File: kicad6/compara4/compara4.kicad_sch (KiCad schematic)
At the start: 67 parts, among them J1 In_1, J2 In_2, J3 In_3, J4 In_4, J5 CV_Jack, J6 Out_OR, J7 Out_NOR, J8 Out_XOR, J9 Out_XNOR, Q1 BC547, Q2 BC547, Q3 BC547, Q4 BC547, SW1 SW_SPDT, U1 TL074, U2 4070, U3 4041

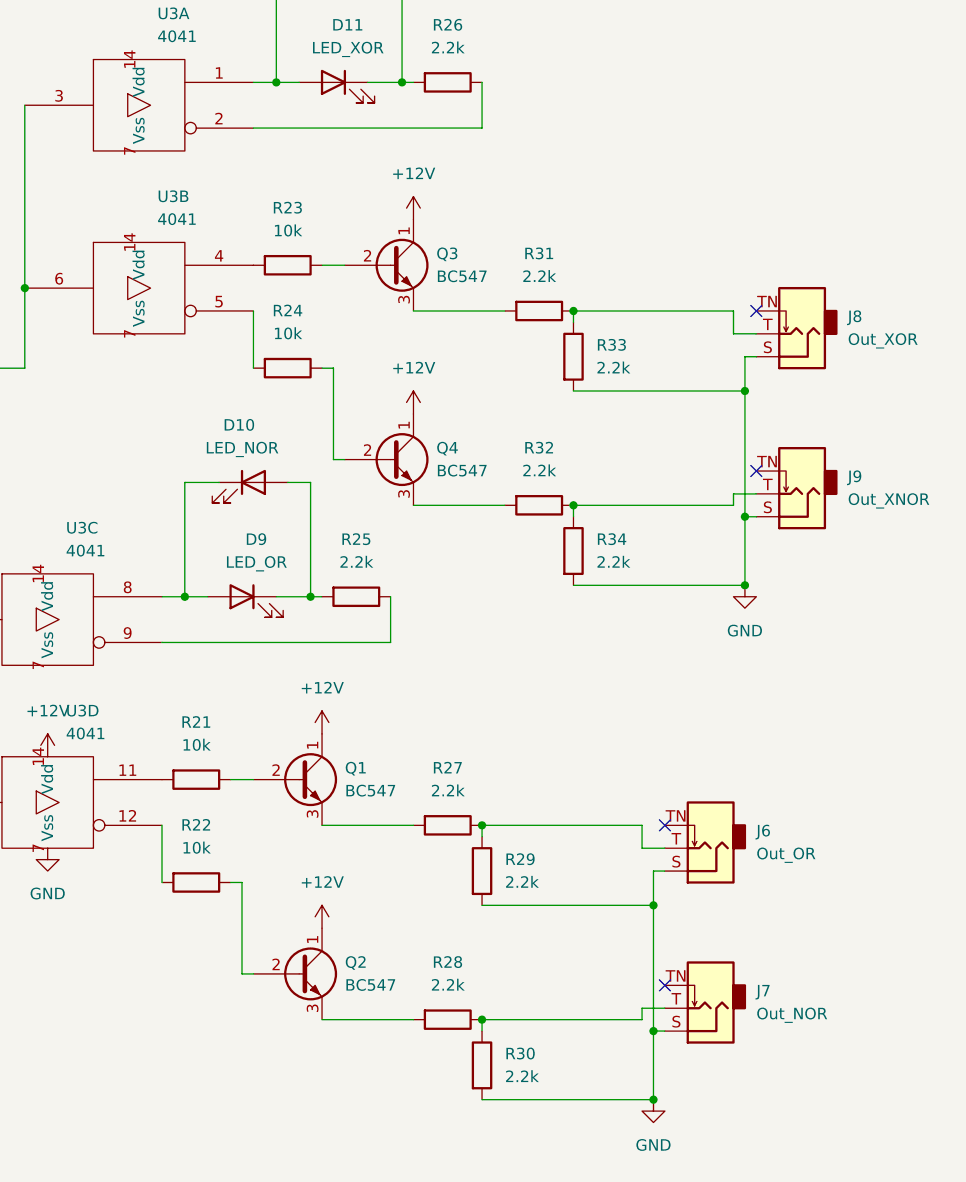
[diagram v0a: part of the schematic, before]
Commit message: Remove transistors from Compara4 schematic
- CD4041 can drive 500 mW total Each LED through 2.2V is about 65 mW
- With potential divider to reduce output voltage, the power numbers for shorts get less scary than through 1k directly.
- If gate output is shorted to ground through 2.2k resistor, it's effectively just another LED - no problem.
- In a worst-case short to -12V, 130mW are drawn from CD4041. This would push it hard but probably not burn it out quickly.
- The resistor between CD4041 and output "sees" twice the voltage drop and passes >1/4W. If this (or an additional low-value series resistor) is specified as a 1/8W then it could act as an additional protection "fuse".
- Probably unnecessary as we don't expect to see simultanous shorts to -12V.
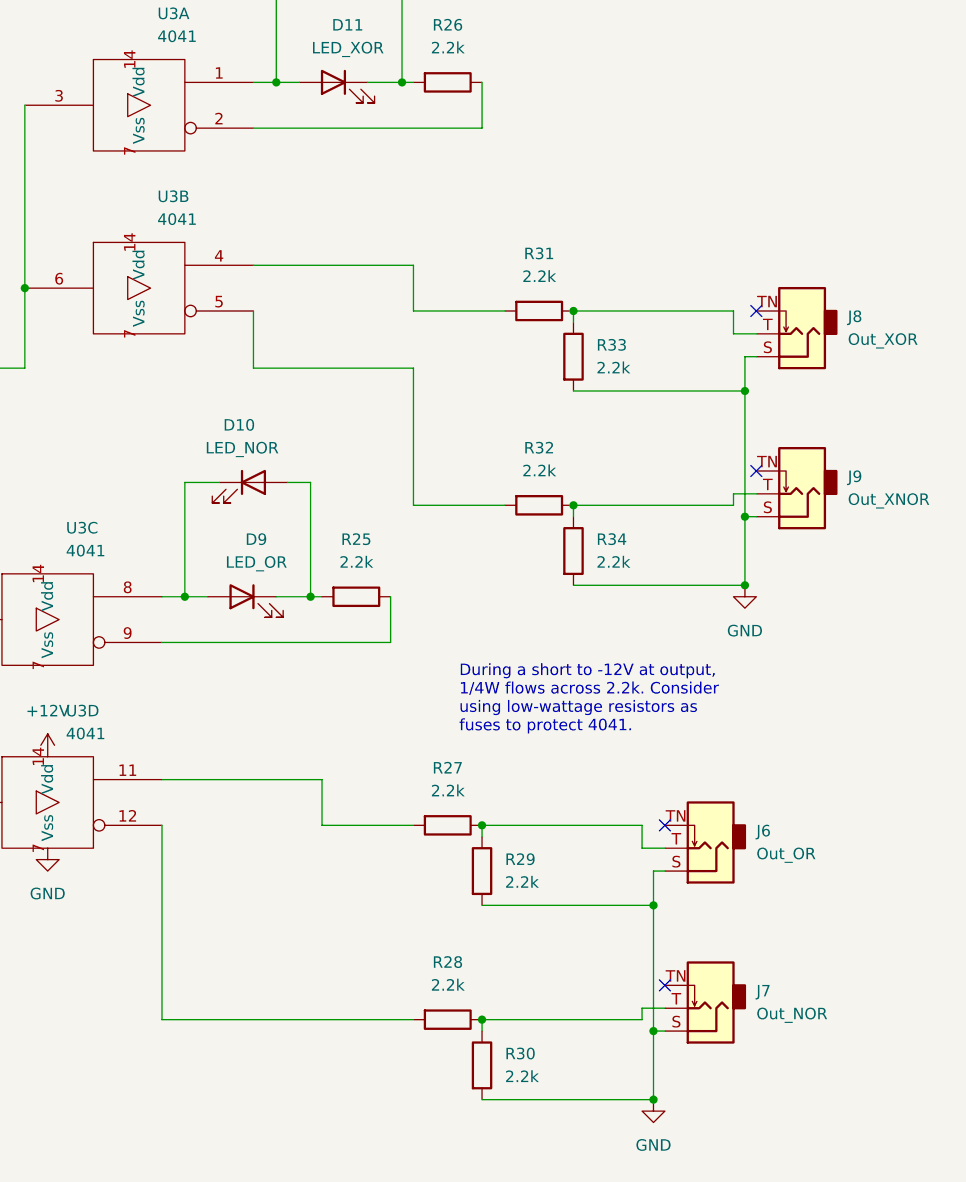
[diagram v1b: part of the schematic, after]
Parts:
- removed Q1, Q2, Q3, Q4: BC547, Package_TO_SOT_THT:TO-92_Inline, symbol Transistor_BJT:BC547
- removed R21, R22, R23, R24: 10k, Resistor_THT:R_Axial_DIN0207_L6.3mm_D2.5mm_P7.62mm_Horizontal, symbol Device:R
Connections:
- net at R32.2: now also U3.5
- net at R31.2: now also U3.4
- net at R28.2: now also U3.12
- net at R27.2: now also U3.11
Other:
- note added: "During a short to -12V at output, 1/4W flows across 2.2k. Consider using low-wattage resistors as fuses to protect 4041."

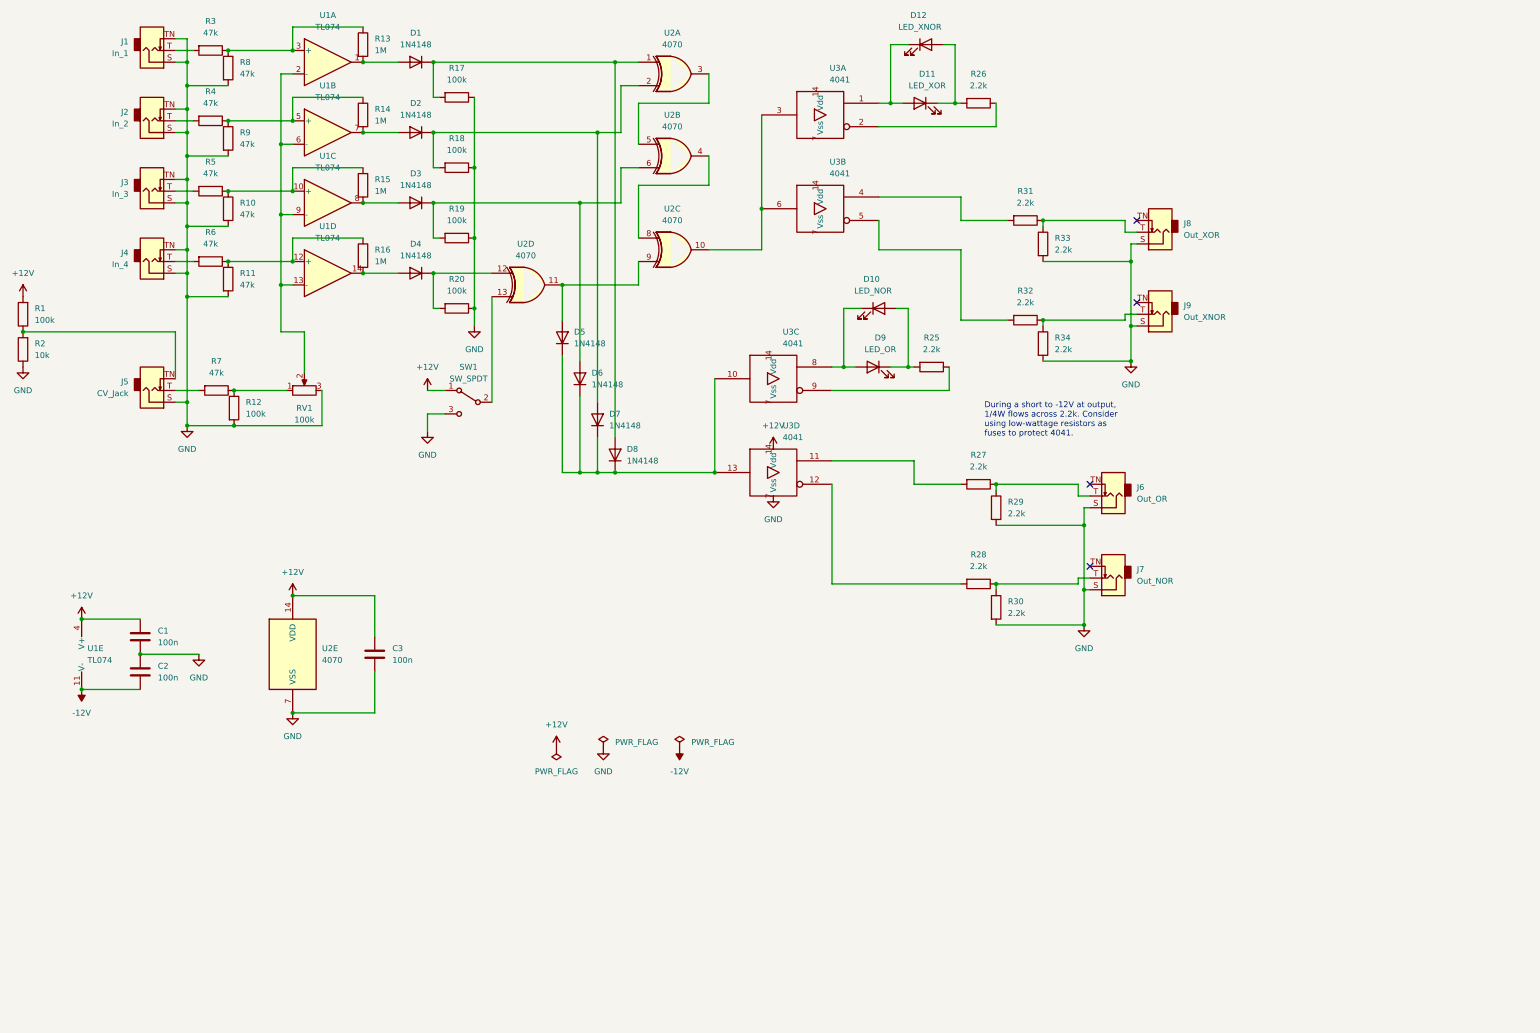
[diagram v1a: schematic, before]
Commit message: compara4; breakout controls, layout for perfboard
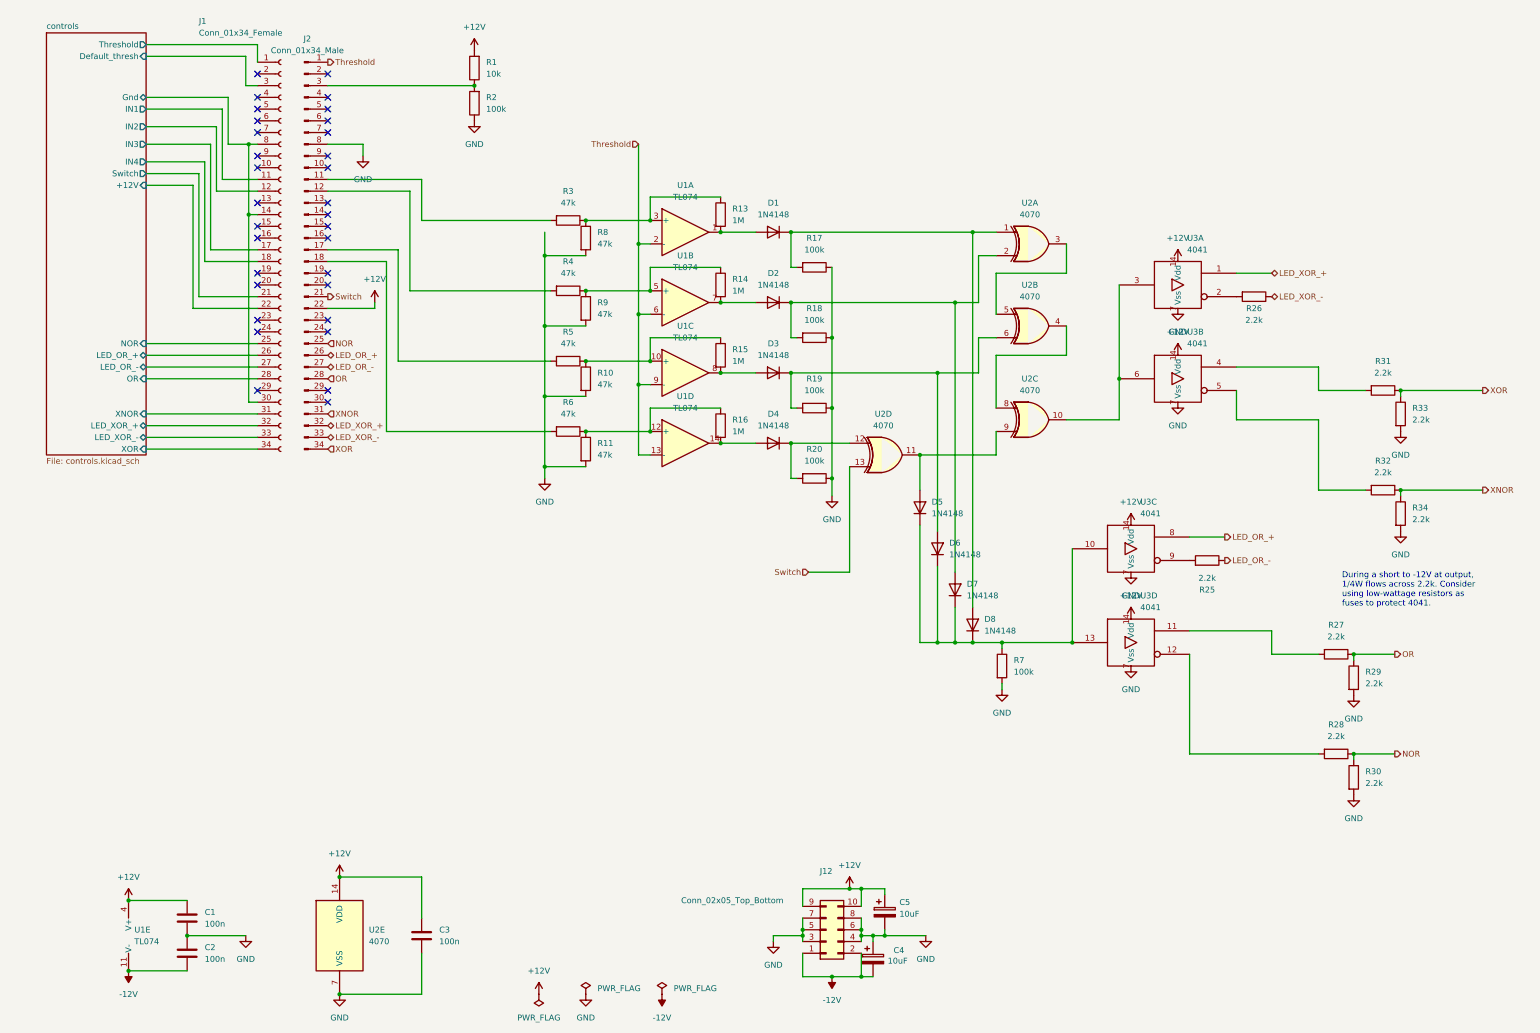
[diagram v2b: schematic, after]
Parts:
- removed D10: LED_NOR, LED_THT:LED_D3.0mm_FlatTop, symbol Device:LED
- removed D11: LED_XOR, LED_THT:LED_D3.0mm_FlatTop, symbol Device:LED
- removed D12: LED_XNOR, LED_THT:LED_D3.0mm_FlatTop, symbol Device:LED
- removed D9: LED_OR, LED_THT:LED_D3.0mm_FlatTop, symbol Device:LED
- removed J1: In_1, Connector_Audio:Jack_3.5mm_QingPu_WQP-PJ398SM_Vertical_CircularHoles, symbol Connector:AudioJack2_SwitchT
- removed J2: In_2, Connector_Audio:Jack_3.5mm_QingPu_WQP-PJ398SM_Vertical_CircularHoles, symbol Connector:AudioJack2_SwitchT
- removed J3: In_3, Connector_Audio:Jack_3.5mm_QingPu_WQP-PJ398SM_Vertical_CircularHoles, symbol Connector:AudioJack2_SwitchT
- removed J4: In_4, Connector_Audio:Jack_3.5mm_QingPu_WQP-PJ398SM_Vertical_CircularHoles, symbol Connector:AudioJack2_SwitchT
- removed J5: CV_Jack, Connector_Audio:Jack_3.5mm_QingPu_WQP-PJ398SM_Vertical_CircularHoles, symbol Connector:AudioJack2_SwitchT
- removed J6: Out_OR, Connector_Audio:Jack_3.5mm_QingPu_WQP-PJ398SM_Vertical_CircularHoles, symbol Connector:AudioJack2_SwitchT
- removed J7: Out_NOR, Connector_Audio:Jack_3.5mm_QingPu_WQP-PJ398SM_Vertical_CircularHoles, symbol Connector:AudioJack2_SwitchT
- removed J8: Out_XOR, Connector_Audio:Jack_3.5mm_QingPu_WQP-PJ398SM_Vertical_CircularHoles, symbol Connector:AudioJack2_SwitchT
- removed J9: Out_XNOR, Connector_Audio:Jack_3.5mm_QingPu_WQP-PJ398SM_Vertical_CircularHoles, symbol Connector:AudioJack2_SwitchT
- removed R12: 100k, Resistor_THT:R_Axial_DIN0207_L6.3mm_D2.5mm_P7.62mm_Horizontal, symbol Device:R
- removed RV1: 100k, Potentiometer_THT:Potentiometer_Alpha_RD901F-40-00D_Single_Vertical, symbol Device:R_Potentiometer
- removed SW1: SW_SPDT, Library:Dailywell sub-miniature toggle switch, symbol Switch:SW_SPDT
- added C4, C5: 10uF, Capacitor_THT:CP_Radial_D5.0mm_P2.50mm, symbol Device:C_Polarized
- added J1: Conn_01x34_Female, Connector_PinHeader_2.54mm:PinHeader_1x34_P2.54mm_Vertical, symbol Connector:Conn_01x34_Female
- added J12: Conn_02x05_Top_Bottom, Connector_IDC:IDC-Header_2x05_P2.54mm_Vertical, symbol Connector_Generic:Conn_02x05_Odd_Even
- added J2: Conn_01x34_Male, Connector_PinHeader_2.54mm:PinHeader_1x34_P2.54mm_Horizontal, symbol Connector:Conn_01x34_Male
- R1: value 100k -> 10k
- R2: value 10k -> 100k
- R7: value 47k -> 100k
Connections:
- net +12V: now also U3.14 (Vdd), U3.14 (Vdd), U3.14 (Vdd), C5.1, J12.10 (Pin_10), J12.9 (Pin_9), J2.22 (Pin_22)
- net -12V: now also C4.2, J12.1 (Pin_1), J12.2 (Pin_2)
- net GND: now also R7.2, U3.7 (Vss), U3.7 (Vss), U3.7 (Vss), C4.1, C5.2, J12.3 (Pin_3), J12.4 (Pin_4), J12.5 (Pin_5), J12.6 (Pin_6), J12.7 (Pin_7), J12.8 (Pin_8), J2.8 (Pin_8)
- net XNOR: now reaches R32.1, R34.1
- net XNOR: now also J2.31 (Pin_31)
- net LED_XOR_+: now reaches U3.1
- net LED_XOR_+: now also J2.32 (Pin_32)
- net at R26.2: now also U3.2
- net at D5.1 (K), D6.1 (K), D7.1 (K)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: now also R7.1
- net XOR: now reaches R31.1, R33.1
- net XOR: now also J2.34 (Pin_34)
- net NOR: now reaches R28.1, R30.1
- net NOR: now also J2.25 (Pin_25)
- net Switch: now reaches U2.13
- net Switch: now also J2.21 (Pin_21)
- net Threshold: now reaches U1.13 (-), U1.2 (-), U1.6 (-), U1.9 (-)
- net Threshold: now also J2.1 (Pin_1)
- net OR: now reaches R27.1, R29.1
- net OR: now also J2.28 (Pin_28)
- net at R1.1, R2.2: now also J2.3 (Pin_3)
- net at R4.2: now also J2.12 (Pin_12)
- net at R6.2: now also J2.18 (Pin_18)
- net at R5.2: now also J2.17 (Pin_17)
- net LED_OR_+: now reaches U3.8
- net LED_OR_+: now also J2.26 (Pin_26)
- net at R25.2: now also U3.9
- net at R3.2: now also J2.11 (Pin_11)
- net LED_OR_-: now reaches R25.1
- net LED_OR_-: now also J2.27 (Pin_27); no longer U3.9
- net LED_XOR_-: now reaches R26.1
- net LED_XOR_-: now also J2.33 (Pin_33); no longer U3.2
- new net controls/+12V: J1.22 (Pin_22)
- new net controls/Default_thresh: J1.3 (Pin_3)
- new net controls/Gnd: J1.14 (Pin_14), J1.30 (Pin_30), J1.8 (Pin_8)
- new net controls/IN1: J1.11 (Pin_11)
- new net controls/IN2: J1.12 (Pin_12)
- new net controls/IN3: J1.17 (Pin_17)
- new net controls/IN4: J1.18 (Pin_18)
- new net controls/LED_OR_+: J1.26 (Pin_26)
- new net controls/LED_OR_-: J1.27 (Pin_27)
- new net controls/LED_XOR_+: J1.32 (Pin_32)
- new net controls/LED_XOR_-: J1.33 (Pin_33)
- new net controls/NOR: J1.25 (Pin_25)
- new net controls/OR: J1.28 (Pin_28)
- new net controls/Switch: J1.21 (Pin_21)
- new net controls/Threshold: J1.1 (Pin_1)
- new net controls/XNOR: J1.31 (Pin_31)
- new net controls/XOR: J1.34 (Pin_34)
- no-connect marks 4 -> 32
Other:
- added sheet controls (controls.kicad_sch)
- moved on the sheet: C1, C2, C3, D1, D2, D3, D4, D5, D6, D7, D8, R1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

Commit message: compara4: reverse pot and cleanup ERC
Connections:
- net controls/Gnd: now also J1.24 (Pin_24)
- no-connect marks 32 -> 31
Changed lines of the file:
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@@
   (junction (at 212.09 120.65) (diameter 0) (color 0 0 0 0)
+  )
+  (junction (at 66.675 93.98) (diameter 0) (color 0 0 0 0)
   )
   (junction (at 153.67 85.09) (diameter 0) (color 0 0 0 0)
@@
   (no_connect (at 68.58 50.8))
   (no_connect (at 83.82 43.18))
-  (no_connect (at 68.58 93.98))
   (no_connect (at 68.58 66.04))
   (no_connect (at 68.58 38.1))
@@
     (stroke (width 0) (type default) (color 0 0 0 0))
   )
+  (wire (pts (xy 66.675 93.98) (xy 68.58 93.98))
+    (stroke (width 0) (type default) (color 0 0 0 0))
+  )
   (wire (pts (xy 58.42 76.2) (xy 68.58 76.2))
     (stroke (width 0) (type default) (color 0 0 0 0))
@@
     (stroke (width 0) (type default) (color 0 0 0 0))
   )
-  (wire (pts (xy 66.675 68.58) (xy 66.675 109.22))
+  (wire (pts (xy 66.675 68.58) (xy 66.675 93.98))
     (stroke (width 0) (type default) (color 0 0 0 0))
   )
@@
     (stroke (width 0) (type default) (color 0 0 0 0))
   )
+  (wire (pts (xy 66.675 93.98) (xy 66.675 109.22))
+    (stroke (width 0) (type default) (color 0 0 0 0))
+  )

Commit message: compara4; alignment corrections, some jumper cleanup
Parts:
- added R22: 10k, Resistor_THT:R_Axial_DIN0207_L6.3mm_D2.5mm_P7.62mm_Horizontal, symbol Device:R
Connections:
- net +12V: now also R22.1; no longer J2.22 (Pin_22)
- new net: J2.22 (Pin_22), R22.2
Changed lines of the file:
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@@
+    (stroke (width 0) (type default) (color 0 0 0 0))
+  )
+  (wire (pts (xy 92.71 88.9) (xy 93.98 88.9))
     (stroke (width 0) (type default) (color 0 0 0 0))
   )
@@
     (stroke (width 0) (type default) (color 0 0 0 0))
   )
+  (wire (pts (xy 83.82 88.9) (xy 85.09 88.9))
+    (stroke (width 0) (type default) (color 0 0 0 0))
+  )
   (wire (pts (xy 57.15 57.15) (xy 57.15 78.74))
     (stroke (width 0) (type default) (color 0 0 0 0))
@@
   )
   (wire (pts (xy 199.39 223.52) (xy 199.39 224.79))
-    (stroke (width 0) (type default) (color 0 0 0 0))
-  )
-  (wire (pts (xy 83.82 88.9) (xy 93.98 88.9))
     (stroke (width 0) (type default) (color 0 0 0 0))
   )
@@
     )
     (pin "1")
+  )
+  (symbol (lib_id "Device:R") (at 88.9 88.9 270) (unit 1)
+    (in_bom yes) (on_board yes)
+    (property "Reference" "R22" (id 0) (at 88.9 88.9 90))
+    (property "Value" "10k" (id 1) (at 88.9 91.44 90))
+    (property "Footprint" "Resistor_THT:R_Axial_DIN0207_L6.3mm_D2.5mm_P7.62mm_Horizontal" (id 2) (at 88.9 87.122 90)
+      (effects (font (size 1.27 1.27)) hide)
+    )
+    (property "Datasheet" "~" (id 3) (at 88.9 88.9 0)
+      (effects (font (size 1.27 1.27)) hide)
+    )
+    (pin "1")
+    (pin "2")
   )
   (symbol (lib_id "4xxx:4070") (at 236.22 92.71 0) (unit 2)
@@
       (reference "R21") (unit 1) (value "100k") (footprint "Resistor_THT:R_Axial_DIN0207_L6.3mm_D2.5mm_P7.62mm_Horizontal")
     )
+    (path "/022d6a78-132a-497b-bdd2-2373cf73d377"
+      (reference "R22") (unit 1) (value "10k") (footprint "Resistor_THT:R_Axial_DIN0207_L6.3mm_D2.5mm_P7.62mm_Horizontal")
+    )
     (path "/b2a63bbc-913b-427f-9aa7-7c1c11576efa"
